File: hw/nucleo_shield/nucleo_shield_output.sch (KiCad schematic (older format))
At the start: 13 parts, among them P10 CONN_OUTH1, P11 CONN_OUTH2, P14 CONN_OUT2, P2 CONN_OUT3, P3 CONN_OUT1, P8 CONN_OUT4, U1 74HC595, U10 ULN2803, U11 74HC595, U12 74HC595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

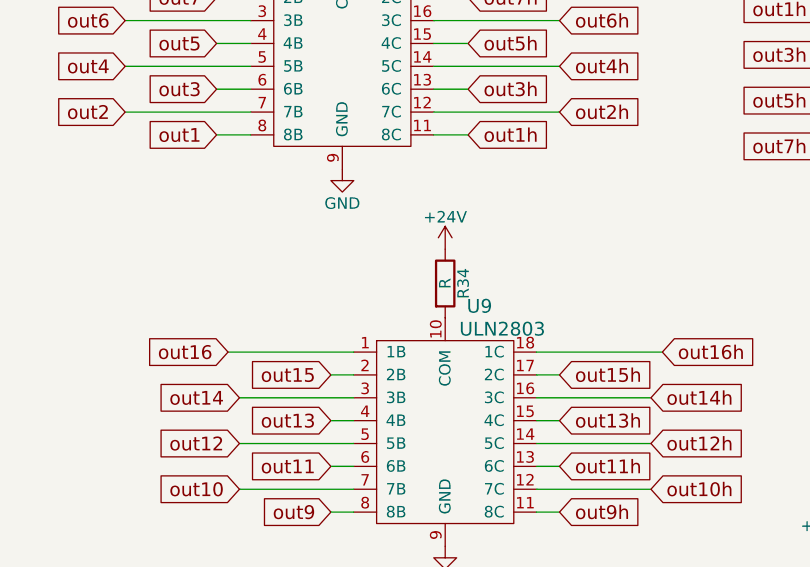
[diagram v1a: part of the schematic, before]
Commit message: Nucleo: Add mounting holes, add more spacing between tracks
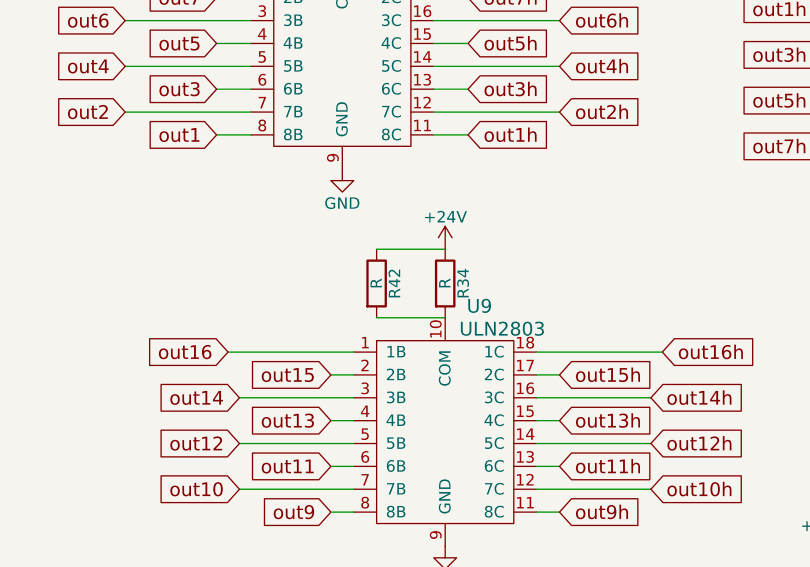
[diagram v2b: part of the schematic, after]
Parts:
- added R42: R, Resistors_ThroughHole:Resistor_Horizontal_RM10mm, symbol R
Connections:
- net +24V: now also R42.1
- net at R34.2, U9.10 (COM): now also R42.2
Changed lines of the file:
@@
 LIBS:memory
 LIBS:xilinx
-LIBS:special
 LIBS:microcontrollers
 LIBS:dsp
@@
 $EndComp
 $Comp
-L GND #PWR31
+L GND #PWR027
 U 1 1 5729AB4A
 P 1500 1900
-F 0 "#PWR31" H 1500 1650 50  0001 C CNN
+F 0 "#PWR027" H 1500 1650 50  0001 C CNN
 F 1 "GND" H 1500 1750 50  0000 C CNN
 F 2 "" H 1500 1900 60  0000 C CNN
@@
 $EndComp
 $Comp
-L GND #PWR32
+L GND #PWR028
 U 1 1 5729AB50
 P 1500 3500
-F 0 "#PWR32" H 1500 3250 50  0001 C CNN
+F 0 "#PWR028" H 1500 3250 50  0001 C CNN
 F 1 "GND" H 1500 3350 50  0000 C CNN
 F 2 "" H 1500 3500 60  0000 C CNN
@@
 $EndComp
 $Comp
-L +5V #PWR35
+L +5V #PWR029
 U 1 1 5729ABD5
 P 1900 750
-F 0 "#PWR35" H 1900 600 50  0001 C CNN
+F 0 "#PWR029" H 1900 600 50  0001 C CNN
 F 1 "+5V" H 1900 890 50  0000 C CNN
 F 2 "" H 1900 750 60  0000 C CNN
@@
 $EndComp
 $Comp
-L +5V #PWR36
+L +5V #PWR030
 U 1 1 5729ABDB
 P 3600 2400
-F 0 "#PWR36" H 3600 2250 50  0001 C CNN
+F 0 "#PWR030" H 3600 2250 50  0001 C CNN
 F 1 "+5V" H 3600 2540 50  0000 C CNN
 F 2 "" H 3600 2400 60  0000 C CNN
@@
 $EndComp
 $Comp
-L +5V #PWR30
+L +5V #PWR031
 U 1 1 5729ABE8
 P 1350 1450
-F 0 "#PWR30" H 1350 1300 50  0001 C CNN
+F 0 "#PWR031" H 1350 1300 50  0001 C CNN
 F 1 "+5V" H 1350 1590 50  0000 C CNN
 F 2 "" H 1350 1450 60  0000 C CNN
@@
 $EndComp
 $Comp
-L +5V #PWR27
+L +5V #PWR032
 U 1 1 5729ABEE
 P 1100 2950
-F 0 "#PWR27" H 1100 2800 50  0001 C CNN
+F 0 "#PWR032" H 1100 2800 50  0001 C CNN
 F 1 "+5V" H 1100 3090 50  0000 C CNN
 F 2 "" H 1100 2950 60  0000 C CNN
@@
 $EndComp
 $Comp
-L GND #PWR48
+L GND #PWR033
 U 1 1 57307D6B
 P 7150 1750
-F 0 "#PWR48" H 7150 1500 50  0001 C CNN
+F 0 "#PWR033" H 7150 1500 50  0001 C CNN
 F 1 "GND" H 7150 1600 50  0000 C CNN
 F 2 "" H 7150 1750 60  0000 C CNN
@@
 $EndComp
 $Comp
-L GND #PWR50
+L GND #PWR034
 U 1 1 57307D82
 P 7600 3400
-F 0 "#PWR50" H 7600 3150 50  0001 C CNN
+F 0 "#PWR034" H 7600 3150 50  0001 C CNN
 F 1 "GND" H 7600 3250 50  0000 C CNN
 F 2 "" H 7600 3400 60  0000 C CNN
@@
 $EndComp
 $Comp
-L +24V #PWR47
+L +24V #PWR035
 U 1 1 57307DA1
 P 7150 750
-F 0 "#PWR47" H 7150 600 50  0001 C CNN
+F 0 "#PWR035" H 7150 600 50  0001 C CNN
 F 1 "+24V" H 7150 890 50  0000 C CNN
 F 2 "" H 7150 750 60  0000 C CNN
@@
 out8h
 $Comp
-L GND #PWR52
+L GND #PWR036
 U 1 1 573085F0
 P 9400 900
-F 0 "#PWR52" H 9400 650 50  0001 C CNN
+F 0 "#PWR036" H 9400 650 50  0001 C CNN
 F 1 "GND" H 9400 750 50  0000 C CNN
 F 2 "" H 9400 900 60  0000 C CNN
@@
 $EndComp
 $Comp
-L GND #PWR53
+L GND #PWR037
 U 1 1 5730860B
 P 9550 3350
-F 0 "#PWR53" H 9550 3100 50  0001 C CNN
+F 0 "#PWR037" H 9550 3100 50  0001 C CNN
 F 1 "GND" H 9550 3200 50  0000 C CNN
 F 2 "" H 9550 3350 60  0000 C CNN
@@
 $EndComp
 $Comp
-L +24V #PWR54
+L +24V #PWR038
 U 1 1 573087B8
 P 9700 700
-F 0 "#PWR54" H 9700 550 50  0001 C CNN
+F 0 "#PWR038" H 9700 550 50  0001 C CNN
 F 1 "+24V" H 9700 840 50  0000 C CNN
 F 2 "" H 9700 700 60  0000 C CNN
@@
 $EndComp
 $Comp
-L +24V #PWR51
+L +24V #PWR039
 U 1 1 5730884E
 P 9250 3450
-F 0 "#PWR51" H 9250 3300 50  0001 C CNN
+F 0 "#PWR039" H 9250 3300 50  0001 C CNN
 F 1 "+24V" H 9250 3590 50  0000 C CNN
 F 2 "" H 9250 3450 60  0000 C CNN
@@
 $EndComp
 $Comp
-L GND #PWR41
+L GND #PWR040
 U 1 1 57326CAA
 P 4900 4250
-F 0 "#PWR41" H 4900 4000 50  0001 C CNN
+F 0 "#PWR040" H 4900 4000 50  0001 C CNN
 F 1 "GND" H 4900 4100 50  0000 C CNN
 F 2 "" H 4900 4250 60  0000 C CNN
@@
 out24
 $Comp
-L +5V #PWR44
+L +5V #PWR041
 U 1 1 57326EE3
 P 5200 4050
-F 0 "#PWR44" H 5200 3900 50  0001 C CNN
+F 0 "#PWR041" H 5200 3900 50  0001 C CNN
 F 1 "+5V" H 5200 4190 50  0000 C CNN
 F 2 "" H 5200 4050 60  0000 C CNN
@@
 $EndComp
 $Comp
-L +5V #PWR37
+L +5V #PWR042
 U 1 1 57326A3F
 P 3600 4000
-F 0 "#PWR37" H 3600 3850 50  0001 C CNN
+F 0 "#PWR042" H 3600 3850 50  0001 C CNN
 F 1 "+5V" H 3600 4140 50  0000 C CNN
 F 2 "" H 3600 4000 60  0000 C CNN
@@
 	5300 4400 4650 4400
 $Comp
-L +5V #PWR28
+L +5V #PWR043
 U 1 1 57326A4A
 P 1100 4550
-F 0 "#PWR28" H 1100 4400 50  0001 C CNN
+F 0 "#PWR043" H 1100 4400 50  0001 C CNN
 F 1 "+5V" H 1100 4690 50  0000 C CNN
 F 2 "" H 1100 4550 60  0000 C CNN
@@
 	1200 1250 1200 4450
 $Comp
-L GND #PWR33
+L GND #PWR044
 U 1 1 57326A1D
 P 1500 5100
-F 0 "#PWR33" H 1500 4850 50  0001 C CNN
+F 0 "#PWR044" H 1500 4850 50  0001 C CNN
 F 1 "GND" H 1500 4950 50  0000 C CNN
 F 2 "" H 1500 5100 60  0000 C CNN
@@
 $EndComp
 $Comp
-L GND #PWR39
+L GND #PWR045
 U 1 1 5732DAA7
 P 4850 900
-F 0 "#PWR39" H 4850 650 50  0001 C CNN
+F 0 "#PWR045" H 4850 650 50  0001 C CNN
 F 1 "GND" H 4850 750 50  0000 C CNN
 F 2 "" H 4850 900 60  0000 C CNN
@@
 $EndComp
 $Comp
-L +5V #PWR42
+L +5V #PWR046
 U 1 1 5732DAB5
 P 5150 700
-F 0 "#PWR42" H 5150 550 50  0001 C CNN
+F 0 "#PWR046" H 5150 550 50  0001 C CNN
 F 1 "+5V" H 5150 840 50  0000 C CNN
 F 2 "" H 5150 700 60  0000 C CNN
@@
 $EndComp
 $Comp
-L GND #PWR40
+L GND #PWR047
 U 1 1 5732E01B
 P 4850 2550
-F 0 "#PWR40" H 4850 2300 50  0001 C CNN
+F 0 "#PWR047" H 4850 2300 50  0001 C CNN
 F 1 "GND" H 4850 2400 50  0000 C CNN
 F 2 "" H 4850 2550 60  0000 C CNN
@@
 $EndComp
 $Comp
-L +5V #PWR43
+L +5V #PWR048
 U 1 1 5732E029
 P 5150 2350
-F 0 "#PWR43" H 5150 2200 50  0001 C CNN
+F 0 "#PWR048" H 5150 2200 50  0001 C CNN
 F 1 "+5V" H 5150 2490 50  0000 C CNN
 F 2 "" H 5150 2350 60  0000 C CNN
@@
 	5250 3400 4600 3400
 $Comp
-L +5V #PWR38
+L +5V #PWR049
 U 1 1 5733141E
 P 3600 5600
-F 0 "#PWR38" H 3600 5450 50  0001 C CNN
+F 0 "#PWR049" H 3600 5450 50  0001 C CNN
 F 1 "+5V" H 3600 5740 50  0000 C CNN
 F 2 "" H 3600 5600 60  0000 C CNN
@@
 	2900 5400 2900 5150
 $Comp
-L +5V #PWR29
+L +5V #PWR050
 U 1 1 5733142A
 P 1100 6150
-F 0 "#PWR29" H 1100 6000 50  0001 C CNN
+F 0 "#PWR050" H 1100 6000 50  0001 C CNN
 F 1 "+5V" H 1100 6290 50  0000 C CNN
 F 2 "" H 1100 6150 60  0000 C CNN
@@
 	1200 2850 1200 6050
 $Comp
-L GND #PWR34
+L GND #PWR051
 U 1 1 57331432
 P 1500 6700
-F 0 "#PWR34" H 1500 6450 50  0001 C CNN
+F 0 "#PWR051" H 1500 6450 50  0001 C CNN
 F 1 "GND" H 1500 6550 50  0000 C CNN
 F 2 "" H 1500 6700 60  0000 C CNN
@@
 $EndComp
 $Comp
-L GND #PWR45
+L GND #PWR052
 U 1 1 57331538
 P 5300 5750
-F 0 "#PWR45" H 5300 5500 50  0001 C CNN
+F 0 "#PWR052" H 5300 5500 50  0001 C CNN
 F 1 "GND" H 5300 5600 50  0000 C CNN
 F 2 "" H 5300 5750 60  0000 C CNN
@@
 $EndComp
 $Comp
-L +5V #PWR46
+L +5V #PWR053
 U 1 1 57331546
 P 5600 5550
-F 0 "#PWR46" H 5600 5400 50  0001 C CNN
+F 0 "#PWR053" H 5600 5400 50  0001 C CNN
 F 1 "+5V" H 5600 5690 50  0000 C CNN
 F 2 "" H 5600 5550 60  0000 C CNN
@@
 	5700 5900 5050 5900
 $Comp
-L +24V #PWR49
+L +24V #PWR054
 U 1 1 57334377
 P 7600 2100
-F 0 "#PWR49" H 7600 1950 50  0001 C CNN
+F 0 "#PWR054" H 7600 1950 50  0001 C CNN
 F 1 "+24V" H 7600 2240 50  0000 C CNN
 F 2 "" H 7600 2100 60  0000 C CNN
@@
 	1    0    0    -1
 $EndComp
+$Comp
+L R R42
+U 1 1 5737A3B5
+P 7300 2250
+F 0 "R42" V 7380 2250 50  0000 C CNN
+F 1 "R" V 7300 2250 50  0000 C CNN
+F 2 "Resistors_ThroughHole:Resistor_Horizontal_RM10mm" V 7230 2250 30  0001 C CNN
+F 3 "" H 7300 2250 30  0000 C CNN
+	1    7300 2250
+	1    0    0    -1
+$EndComp
+Wire Wire Line
+	7300 2100 7600 2100
+Wire Wire Line
+	7300 2400 7600 2400
 $EndSCHEMATC

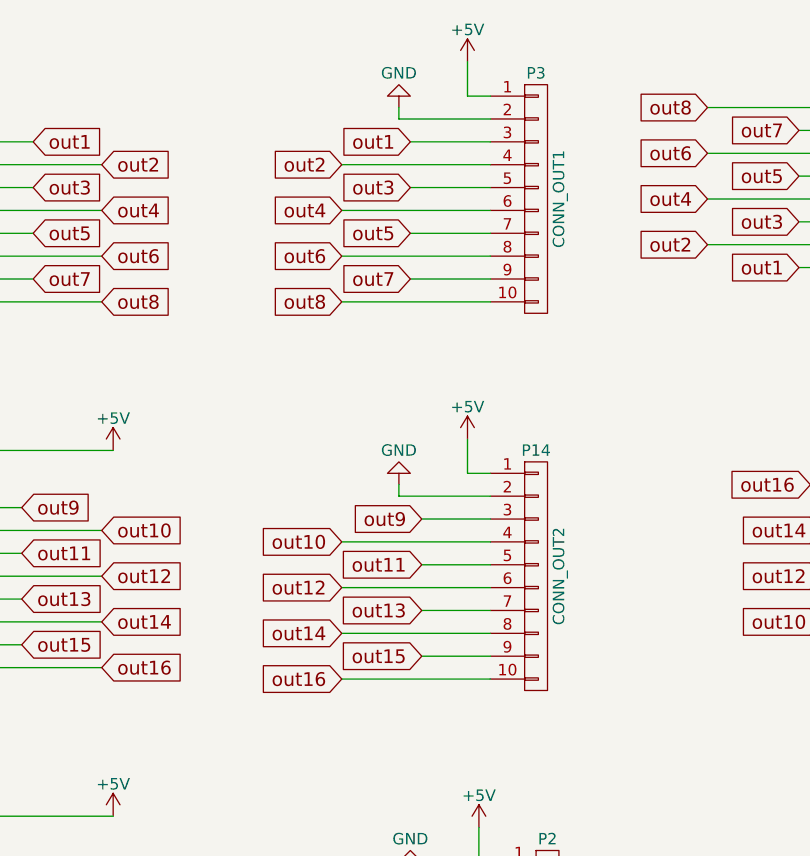
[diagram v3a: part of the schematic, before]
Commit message: Nucleo: update schematic and remove intermediate header for outputs
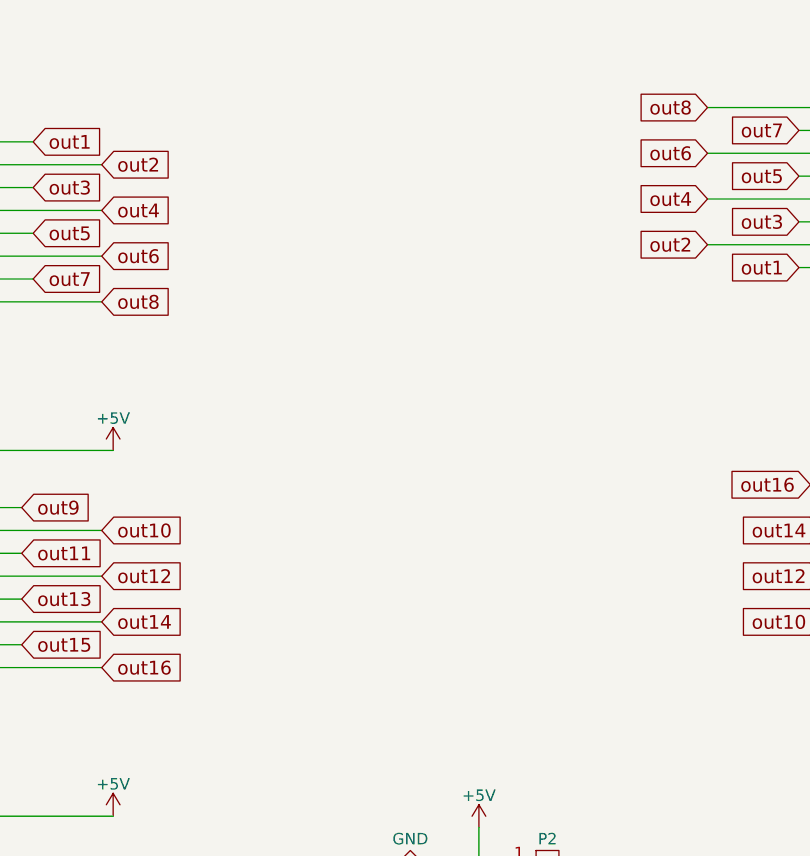
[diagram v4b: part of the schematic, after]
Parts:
- removed P14: CONN_OUT2, Pin_Headers:Pin_Header_Straight_1x10, symbol CONN_01X10
- removed P3: CONN_OUT1, Pin_Headers:Pin_Header_Straight_1x10, symbol CONN_01X10
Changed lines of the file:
@@
 LIBS:memory
 LIBS:xilinx
+LIBS:special
 LIBS:microcontrollers
 LIBS:dsp
@@
 	1500 4250 1500 3800
 $Comp
-L CONN_01X10 P3
-U 1 1 5732DAA1
-P 5450 1300
-F 0 "P3" H 5450 1850 50  0000 C CNN
-F 1 "CONN_OUT1" V 5550 1300 50  0000 C CNN
-F 2 "Pin_Headers:Pin_Header_Straight_1x10" H 5450 1300 60  0001 C CNN
-F 3 "" H 5450 1300 60  0000 C CNN
-	1    5450 1300
-	1    0    0    -1
-$EndComp
-$Comp
-L GND #PWR047
-U 1 1 5732DAA7
-P 4850 900
-F 0 "#PWR047" H 4850 650 50  0001 C CNN
-F 1 "GND" H 4850 750 50  0000 C CNN
-F 2 "" H 4850 900 60  0000 C CNN
-F 3 "" H 4850 900 60  0000 C CNN
-	1    4850 900
-	-1   0    0    1
-$EndComp
-$Comp
-L +5V #PWR048
-U 1 1 5732DAB5
-P 5150 700
-F 0 "#PWR048" H 5150 550 50  0001 C CNN
-F 1 "+5V" H 5150 840 50  0000 C CNN
-F 2 "" H 5150 700 60  0000 C CNN
-F 3 "" H 5150 700 60  0000 C CNN
-	1    5150 700
-	1    0    0    -1
-$EndComp
-Wire Wire Line
-	5250 950  4850 950
-Wire Wire Line
-	4850 950  4850 900
-Wire Wire Line
-	5150 700  5150 850
-Wire Wire Line
-	5150 850  5250 850
-Text GLabel 4900 1050 0    60   Input ~ 0
-out1
-Text GLabel 4600 1150 0    60   Input ~ 0
-out2
-Text GLabel 4900 1250 0    60   Input ~ 0
-out3
-Text GLabel 4600 1350 0    60   Input ~ 0
-out4
-Text GLabel 4900 1450 0    60   Input ~ 0
-out5
-Text GLabel 4600 1550 0    60   Input ~ 0
-out6
-Text GLabel 4900 1650 0    60   Input ~ 0
-out7
-Text GLabel 4600 1750 0    60   Input ~ 0
-out8
-Wire Wire Line
-	5250 1750 4600 1750
-Wire Wire Line
-	5250 1650 4900 1650
-Wire Wire Line
-	5250 1550 4600 1550
-Wire Wire Line
-	4900 1450 5250 1450
-Wire Wire Line
-	5250 1350 4600 1350
-Wire Wire Line
-	5250 1250 4900 1250
-Wire Wire Line
-	5250 1150 4600 1150
-Wire Wire Line
-	5250 1050 4900 1050
-$Comp
-L CONN_01X10 P14
-U 1 1 5732E015
-P 5450 2950
-F 0 "P14" H 5450 3500 50  0000 C CNN
-F 1 "CONN_OUT2" V 5550 2950 50  0000 C CNN
-F 2 "Pin_Headers:Pin_Header_Straight_1x10" H 5450 2950 60  0001 C CNN
-F 3 "" H 5450 2950 60  0000 C CNN
-	1    5450 2950
-	1    0    0    -1
-$EndComp
-$Comp
-L GND #PWR049
-U 1 1 5732E01B
-P 4850 2550
-F 0 "#PWR049" H 4850 2300 50  0001 C CNN
-F 1 "GND" H 4850 2400 50  0000 C CNN
-F 2 "" H 4850 2550 60  0000 C CNN
-F 3 "" H 4850 2550 60  0000 C CNN
-	1    4850 2550
-	-1   0    0    1
-$EndComp
-$Comp
-L +5V #PWR050
-U 1 1 5732E029
-P 5150 2350
-F 0 "#PWR050" H 5150 2200 50  0001 C CNN
-F 1 "+5V" H 5150 2490 50  0000 C CNN
-F 2 "" H 5150 2350 60  0000 C CNN
-F 3 "" H 5150 2350 60  0000 C CNN
-	1    5150 2350
-	1    0    0    -1
-$EndComp
-Wire Wire Line
-	5250 2600 4850 2600
-Wire Wire Line
-	4850 2600 4850 2550
-Wire Wire Line
-	5150 2350 5150 2500
-Wire Wire Line
-	5150 2500 5250 2500
-Text GLabel 4950 2700 0    60   Input ~ 0
-out9
-Text GLabel 4600 2800 0    60   Input ~ 0
-out10
-Text GLabel 4950 2900 0    60   Input ~ 0
-out11
-Text GLabel 4600 3000 0    60   Input ~ 0
-out12
-Text GLabel 4950 3100 0    60   Input ~ 0
-out13
-Text GLabel 4600 3200 0    60   Input ~ 0
-out14
-Text GLabel 4950 3300 0    60   Input ~ 0
-out15
-Text GLabel 4600 3400 0    60   Input ~ 0
-out16
-Wire Wire Line
-	5250 2700 4950 2700
-Wire Wire Line
-	5250 2800 4600 2800
-Wire Wire Line
-	5250 2900 4950 2900
-Wire Wire Line
-	5250 3000 4600 3000
-Wire Wire Line
-	5250 3100 4950 3100
-Wire Wire Line
-	5250 3200 4600 3200
-Wire Wire Line
-	5250 3300 4950 3300
-Wire Wire Line
-	5250 3400 4600 3400
-$Comp
-L +5V #PWR051
+L +5V #PWR047
 U 1 1 5733141E
 P 3600 5600
-F 0 "#PWR051" H 3600 5450 50  0001 C CNN
+F 0 "#PWR047" H 3600 5450 50  0001 C CNN
 F 1 "+5V" H 3600 5740 50  0000 C CNN
 F 2 "" H 3600 5600 60  0000 C CNN
@@
 	2900 5400 2900 5150
 $Comp
-L +5V #PWR052
+L +5V #PWR048
 U 1 1 5733142A
 P 1100 6150
-F 0 "#PWR052" H 1100 6000 50  0001 C CNN
+F 0 "#PWR048" H 1100 6000 50  0001 C CNN
 F 1 "+5V" H 1100 6290 50  0000 C CNN
 F 2 "" H 1100 6150 60  0000 C CNN
@@
 	1200 2850 1200 6050
 $Comp
-L GND #PWR053
+L GND #PWR049
 U 1 1 57331432
 P 1500 6700
-F 0 "#PWR053" H 1500 6450 50  0001 C CNN
+F 0 "#PWR049" H 1500 6450 50  0001 C CNN
 F 1 "GND" H 1500 6550 50  0000 C CNN
 F 2 "" H 1500 6700 60  0000 C CNN
@@
 $EndComp
 $Comp
-L GND #PWR054
+L GND #PWR050
 U 1 1 57331538
 P 5300 5750
-F 0 "#PWR054" H 5300 5500 50  0001 C CNN
+F 0 "#PWR050" H 5300 5500 50  0001 C CNN
 F 1 "GND" H 5300 5600 50  0000 C CNN
 F 2 "" H 5300 5750 60  0000 C CNN
@@
 $EndComp
 $Comp
-L +5V #PWR055
+L +5V #PWR051
 U 1 1 57331546
 P 5600 5550
-F 0 "#PWR055" H 5600 5400 50  0001 C CNN
+F 0 "#PWR051" H 5600 5400 50  0001 C CNN
 F 1 "+5V" H 5600 5690 50  0000 C CNN
 F 2 "" H 5600 5550 60  0000 C CNN
@@
 	5700 5900 5050 5900
 $Comp
-L +24V #PWR056
+L +24V #PWR052
 U 1 1 57334377
 P 7600 2100
-F 0 "#PWR056" H 7600 1950 50  0001 C CNN
+F 0 "#PWR052" H 7600 1950 50  0001 C CNN
 F 1 "+24V" H 7600 2240 50  0000 C CNN
 F 2 "" H 7600 2100 60  0000 C CNN

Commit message: Nucleo: ad vias
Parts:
- removed R34, R42: R, Resistors_ThroughHole:Resistor_Horizontal_RM10mm, symbol R
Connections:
- net +24V: now also U9.10 (COM)
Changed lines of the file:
@@
-	1    0    0    -1
-$EndComp
-$Comp
-L R R34
-U 1 1 57335AE7
-P 7600 2250
-F 0 "R34" V 7680 2250 50  0000 C CNN
-F 1 "R" V 7600 2250 50  0000 C CNN
-F 2 "Resistors_ThroughHole:Resistor_Horizontal_RM10mm" V 7530 2250 30  0001 C CNN
-F 3 "" H 7600 2250 30  0000 C CNN
-	1    7600 2250
-	1    0    0    -1
-$EndComp
-$Comp
-L R R42
-U 1 1 5737A3B5
-P 7300 2250
-F 0 "R42" V 7380 2250 50  0000 C CNN
-F 1 "R" V 7300 2250 50  0000 C CNN
-F 2 "Resistors_ThroughHole:Resistor_Horizontal_RM10mm" V 7230 2250 30  0001 C CNN
-F 3 "" H 7300 2250 30  0000 C CNN
-	1    7300 2250
 	1    0    0    -1
 $EndComp
 Wire Wire Line
-	7300 2100 7600 2100
-Wire Wire Line
-	7300 2400 7600 2400
+	7600 2400 7600 2100
 $EndSCHEMATC

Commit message: WIP: add more IO
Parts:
- P10, P11: footprint w_conn_screw:mors_10p -> w_conn_screw:mors_8p; symbol CONN_01X10 -> CONN_01X08
- P2, P8: footprint Pin_Headers:Pin_Header_Straight_1x10 -> Pin_Headers:Pin_Header_Straight_1x08; symbol CONN_01X10 -> CONN_01X08
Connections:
- net +24V: no longer P10.1 (P1), P11.10 (P10)
- net +5V: no longer P2.1 (P1), P8.1 (P1)
- net GND: no longer P10.2 (P2), P11.9 (P9), P2.2 (P2), P8.2 (P2)
- net SRCLK: no longer U11.11 (SRCLK), U12.11 (SRCLK), U2.11 (SRCLK)
- net SRLatch: no longer U11.12 (RCLK), U12.12 (RCLK), U2.12 (RCLK)
- net out10: now also U11.1 (QB); no longer U2.1 (QB)
- net out11: now also U11.2 (QC); no longer U2.2 (QC)
- net out12: now also U11.3 (QD); no longer U2.3 (QD)
- net out13: now also U11.4 (QE); no longer U2.4 (QE)
- net out14: now also U11.5 (QF); no longer U2.5 (QF)
- net out15: now also U11.6 (QG); no longer U2.6 (QG)
- net out16: now also U11.7 (QH); no longer U2.7 (QH)
- net out17: now also P2.8 (P8), U2.15 (QA); no longer P2.10 (P10), U11.15 (QA)
- net out18: now also P2.7 (P7), U2.1 (QB); no longer P2.9 (P9), U11.1 (QB)
- net out19: now also P2.6 (P6), U2.2 (QC); no longer P2.8 (P8), U11.2 (QC)
- net out1h: now also P10.1 (P1); no longer P10.3 (P3)
- net out20: now also P2.5 (P5), U2.3 (QD); no longer P2.7 (P7), U11.3 (QD)
- net out21: now also P2.4 (P4), U2.4 (QE); no longer P2.6 (P6), U11.4 (QE)
- net out22: now also P2.3 (P3), U2.5 (QF); no longer P2.5 (P5), U11.5 (QF)
- net out23: now also P2.2 (P2), U2.6 (QG); no longer P2.4 (P4), U11.6 (QG)
- net out24: now also P2.1 (P1), U2.7 (QH); no longer P2.3 (P3), U11.7 (QH)
- net out25: now also P8.8 (P8); no longer P8.10 (P10)
- net out26: now also P8.7 (P7); no longer P8.9 (P9)
- net out27: now also P8.6 (P6); no longer P8.8 (P8)
- net out28: now also P8.5 (P5); no longer P8.7 (P7)
- net out29: now also P8.4 (P4); no longer P8.6 (P6)
- net out2h: now also P10.2 (P2); no longer P10.4 (P4)
- net out30: now also P8.3 (P3); no longer P8.5 (P5)
- net out31: now also P8.2 (P2); no longer P8.4 (P4)
- net out32: now also P8.1 (P1); no longer P8.3 (P3)
- net out3h: now also P10.3 (P3); no longer P10.5 (P5)
- net out4h: now also P10.4 (P4); no longer P10.6 (P6)
- net out5h: now also P10.5 (P5); no longer P10.7 (P7)
- net out6h: now also P10.6 (P6); no longer P10.8 (P8)
- net out7h: now also P10.7 (P7); no longer P10.9 (P9)
- net out8h: now also P10.8 (P8); no longer P10.10 (P10)
- net out9: now also U11.15 (QA); no longer U2.15 (QA)
- net at U2.9 (~QH): no longer U11.14 (SER)
- new net SRCLK2: U11.11 (SRCLK), U12.11 (SRCLK)
- new net SRDATA2: U11.14 (SER)
- new net SRLatch2: U11.12 (RCLK), U12.12 (RCLK)
